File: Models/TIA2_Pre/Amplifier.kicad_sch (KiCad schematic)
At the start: 0 parts

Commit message: Save progress
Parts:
- added C1, C2: 1 uF, 0603, symbol Device:C
- added U1: AD8615, symbol Vendor:AD8615
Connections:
- new net -1.5V: C2.1, U1.2 (V-)
- new net 2.5V: C1.1, U1.5 (V+)
- new net GND: C1.2, C2.2

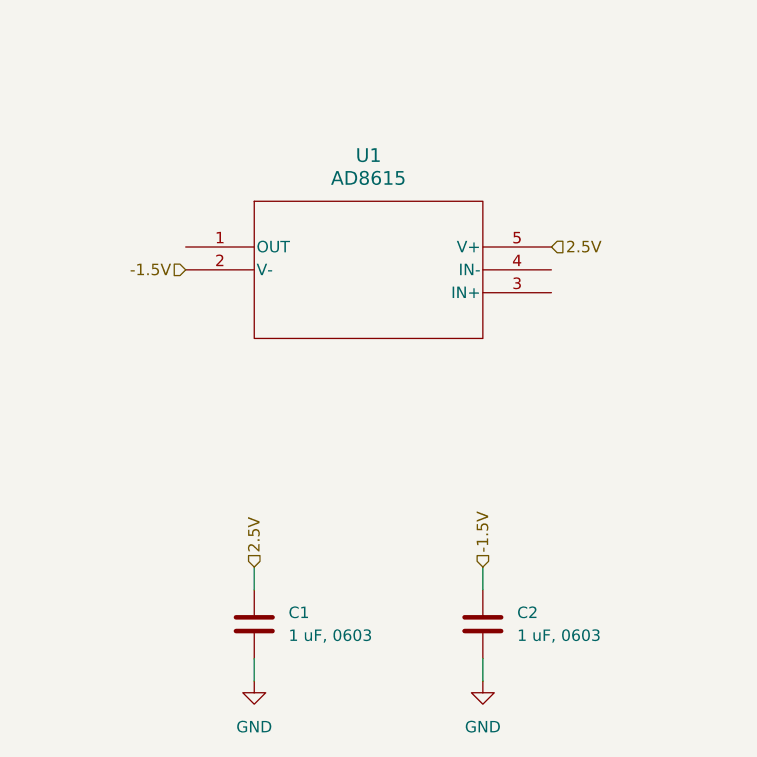
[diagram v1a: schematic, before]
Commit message: Finished with the chips for the transimpedance amplifiers
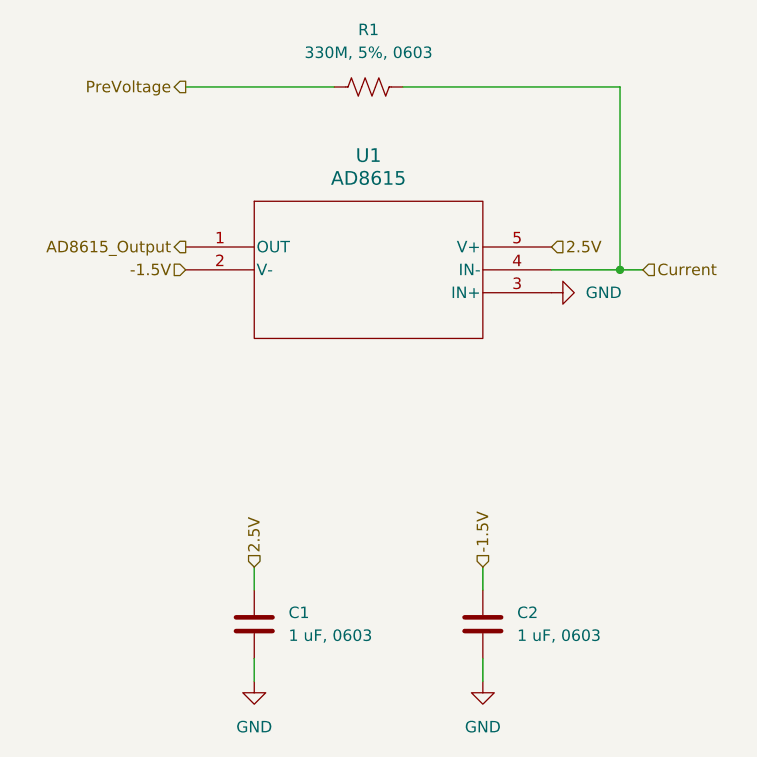
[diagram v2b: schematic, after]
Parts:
- added R1: 330M, 5%, 0603, symbol Device:R_US
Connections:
- net GND: now also U1.3 (IN+)
- net AD8615_Output: now reaches U1.1 (OUT)
- net Current: now reaches U1.4 (IN-)
- net Current: now also R1.2
- new net PreVoltage: R1.1
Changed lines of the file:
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@@
 	(generator_version "9.0")
 	(paper "A4")
+	(junction
+		(at 142.24 83.82)
+		(diameter 0)
+		(color 0 0 0 0)
+	)
 	(wire
 		(pts
@@
 	(wire
 		(pts
+			(xy 142.24 83.82) (xy 144.78 83.82)
+		)
+		(stroke
+			(width 0)
+			(type default)
+		)
+	)
+	(wire
+		(pts
+			(xy 134.62 83.82) (xy 142.24 83.82)
+		)
+		(stroke
+			(width 0)
+			(type default)
+		)
+	)
+	(wire
+		(pts
+			(xy 93.98 63.5) (xy 110.49 63.5)
+		)
+		(stroke
+			(width 0)
+			(type default)
+		)
+	)
+	(wire
+		(pts
 			(xy 101.6 127) (xy 101.6 129.54)
 		)
@@
 			(width 0)
 			(type default)
+		)
+	)
+	(wire
+		(pts
+			(xy 142.24 83.82) (xy 142.24 63.5)
+		)
+		(stroke
+			(width 0)
+			(type default)
+		)
+	)
+	(wire
+		(pts
+			(xy 118.11 63.5) (xy 142.24 63.5)
+		)
+		(stroke
+			(width 0)
+			(type default)
+		)
+	)
+	(hierarchical_label "PreVoltage"
+		(shape output)
+		(at 93.98 63.5 180)
+		(effects
+			(font
+				(size 1.27 1.27)
+			)
+			(justify right)
+		)
+	)
+	(hierarchical_label "AD8615_Output"
+		(shape output)
+		(at 93.98 81.28 180)
+		(effects
+			(font
+				(size 1.27 1.27)
+			)
+			(justify right)
 		)
 	)
@@
 		(shape input)
 		(at 101.6 116.84 90)
+		(effects
+			(font
+				(size 1.27 1.27)
+			)
+			(justify left)
+		)
+	)
+	(hierarchical_label "Current"
+		(shape input)
+		(at 144.78 83.82 0)
 		(effects
 			(font
@@
 					(unit 1)
 				)
+			)
+		)
+	)
+	(symbol
+		(lib_id "Device:R_US")
+		(at 114.3 63.5 90)
+		(unit 1)
+		(exclude_from_sim no)
+		(in_bom yes)
+		(on_board yes)
+		(dnp no)
+		(fields_autoplaced yes)
+		(property "Reference" "R1"
+			(at 114.3 57.15 90)
+			(effects
+				(font
+					(size 1.27 1.27)
+				)
+			)
+		)
+		(property "Value" "330M, 5%, 0603"
+			(at 114.3 59.69 90)
+			(effects
+				(font
+					(size 1.27 1.27)
+				)
+			)
+		)
+		(property "Footprint" ""
+			(at 114.554 62.484 90)
+			(effects
+				(font
+					(size 1.27 1.27)
+				)
+				(hide yes)
+			)
+		)
+		(property "Datasheet" "~"
+			(at 114.3 63.5 0)
+			(effects
+				(font
+					(size 1.27 1.27)
+				)
+				(hide yes)
+			)
+		)
+		(property "Description" "Resistor, US symbol"
+			(at 114.3 63.5 0)
+			(effects
+				(font
+					(size 1.27 1.27)
+				)
+				(hide yes)
+			)
+		)
+		(property "Purchase Link" "https://www.digikey.com/en/products/detail/vishay-dale/CRCW0603330MJPEAHR/5072104"
+			(at 114.3 63.5 0)
+			(effects
+				(font
+					(size 1.27 1.27)
+				)
+				(hide yes)
+			)
+		)
+		(pin "1"
+		)
+		(pin "2"
+		)
+		(instances
+			(project "TIA2_Pre"
+				(path "/f19129fc-f916-4692-924c-ee308c6b3e1d/576e9362-b988-409f-82c5-0c80cb18568a"
+					(reference "R1")
+					(unit 1)
+				)
+			)
+		)
+	)
+	(symbol
+		(lib_id "power:GND")
+		(at 134.62 86.36 90)
+		(unit 1)
+		(exclude_from_sim no)
+		(in_bom yes)
+		(on_board yes)
+		(dnp no)
+		(fields_autoplaced yes)
+		(property "Reference" "#PWR03"
+			(at 140.97 86.36 0)
+			(effects
+				(font
+					(size 1.27 1.27)
+				)
+				(hide yes)
+			)
+		)
+		(property "Value" "GND"
+			(at 138.43 86.3599 90)
+			(effects
+				(font
+					(size 1.27 1.27)
+				)
+				(justify right)
+			)
+		)
+		(property "Footprint" ""
+			(at 134.62 86.36 0)
+			(effects
+				(font
+					(size 1.27 1.27)
+				)
+				(hide yes)
+			)
+		)
+		(property "Datasheet" ""
+			(at 134.62 86.36 0)
+			(effects
+				(font
+					(size 1.27 1.27)
+				)
+				(hide yes)
+			)
+		)
+		(property "Description" "Power symbol creates a global label with name \"GND\" , ground"
+			(at 134.62 86.36 0)
+			(effects
+				(font
+					(size 1.27 1.27)
+				)
+				(hide yes)
+			)
+		)
+		(pin "1"
+		)
+		(instances
+			(project ""
+				(path "/f19129fc-f916-4692-924c-ee308c6b3e1d/576e9362-b988-409f-82c5-0c80cb18568a"
+					(reference "#PWR03")
+					(unit 1)
+				)

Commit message: Save progress
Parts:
- removed R1: 330M, 5%, 0603, symbol Device:R_US
- removed U1: AD8615, symbol Vendor:AD8615
- added R2: 330M, 5%, 0603, symbol Device:R_US
- added U1: AD8615, symbol Amplifier_Operational:OP179GRT
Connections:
- net -1.5V: now also U1.5 (V-)
- net 2.5V: now also U1.2 (V+)
- net AD8615_Output: now also U1.1
- net Current: now also R2.1, U1.4 (-)
- net GND: now also U1.3 (+)
- net PreVoltage: now also R2.2
